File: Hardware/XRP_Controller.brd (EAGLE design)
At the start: 63.5 x 54 mm, 194 parts, among them J1 POWER_JACKPOWER_JACK_SLOT, J12 Vertical Qwiic Connector, J13 Vertical Qwiic Connector, J14 Vertical Qwiic Connector, J3 JST_6_PIN_VERTICAL, J4 JST_6_PIN_VERTICAL, J5 JST_6_PIN_VERTICAL, J6 JST_6_PIN_VERTICAL, J9 Vertical Qwiic Connector, Q3 20V/4.2A/52mΩ/1.4W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

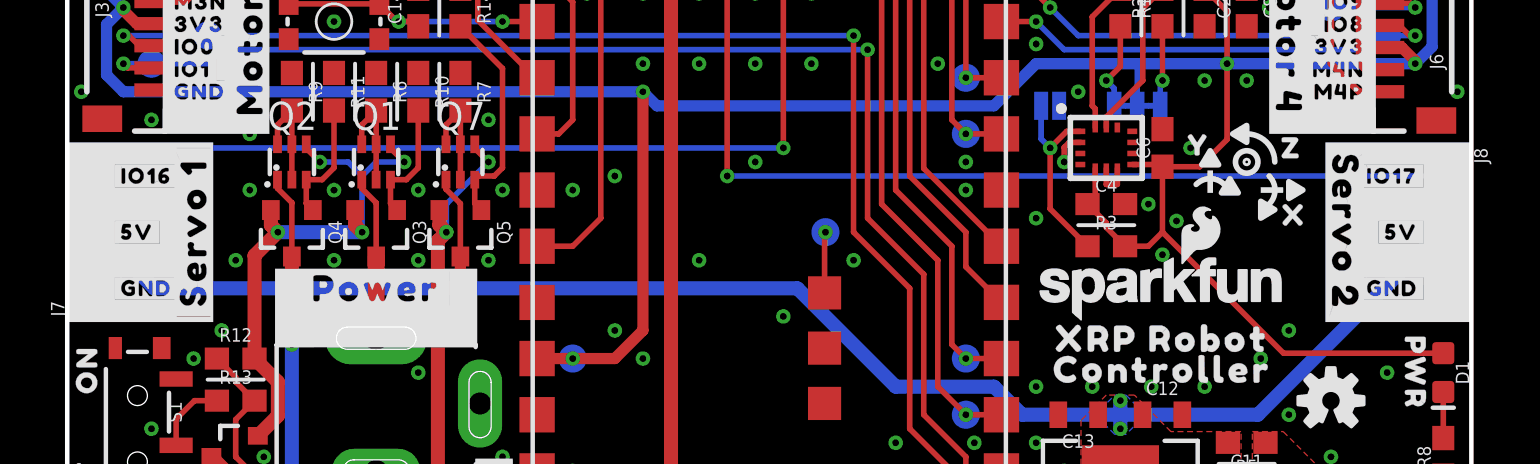
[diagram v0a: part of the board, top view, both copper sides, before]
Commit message: Nudge servo silk to improve readability
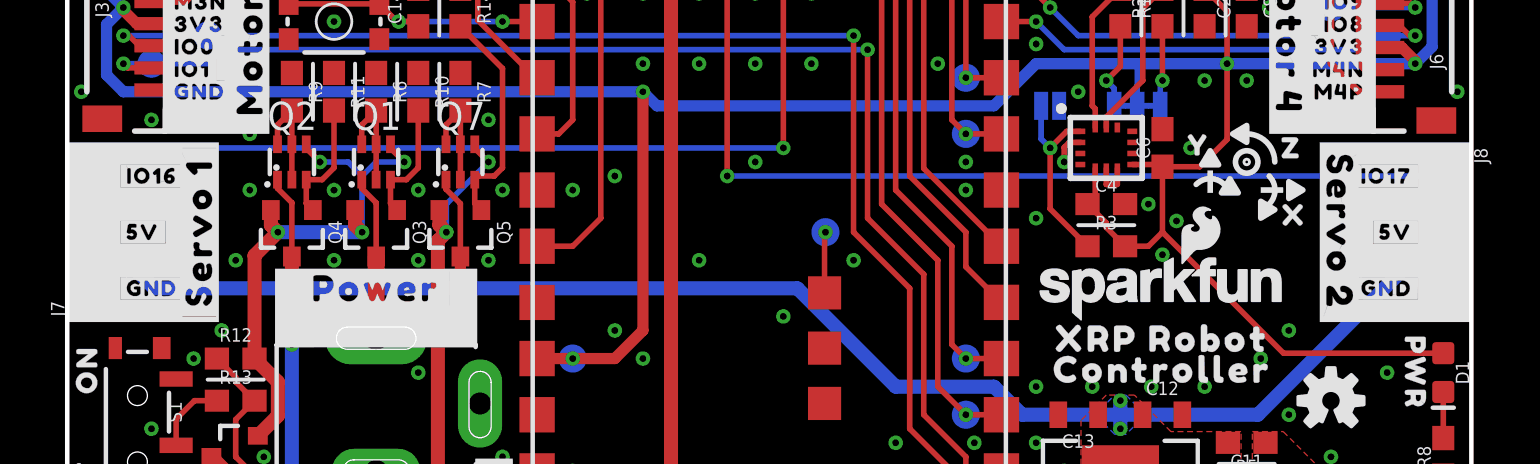
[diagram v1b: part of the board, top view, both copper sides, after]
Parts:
- moved U$11 0.25 mm to (5.97, 19.1)
- moved U$27 0.25 mm to (1.52, 19.1)
- moved U$54 0.25 mm to (2.16, 16.5)
- moved U$55 0.25 mm to (2.16, 19.1)
- moved U$56 0.25 mm to (2.16, 21.6)
- moved U$2 0.25 mm to (57.5, 19.1)
- moved U$57 0.25 mm to (61.3, 16.5)
- moved U$58 0.25 mm to (61.3, 21.6)
- moved U$59 0.25 mm to (61.3, 19.1)
- moved U$76 0.25 mm to (62.0, 19.1)
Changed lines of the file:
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@@
 <drawing>
 <settings>
-<setting alwaysvectorfont="no"/>
+<setting alwaysvectorfont="yes"/>
 <setting verticaltext="up"/>
 </settings>
@@
 <rectangle x1="52.578" y1="48.768" x2="56.642" y2="49.657" layer="21"/>
 <rectangle x1="52.578" y1="45.847" x2="56.642" y2="46.101" layer="21"/>
-<rectangle x1="58.547" y1="22.098" x2="61.341" y2="23.114" layer="21"/>
-<rectangle x1="58.547" y1="14.986" x2="61.341" y2="16.002" layer="21"/>
-<rectangle x1="58.547" y1="19.558" x2="61.341" y2="21.082" layer="21"/>
-<rectangle x1="58.547" y1="17.018" x2="61.341" y2="18.542" layer="21"/>
-<rectangle x1="58.547" y1="18.542" x2="59.309" y2="19.558" layer="21"/>
-<rectangle x1="61.341" y1="14.986" x2="63.5" y2="23.114" layer="21"/>
+<rectangle x1="58.293" y1="22.098" x2="61.087" y2="23.114" layer="21"/>
+<rectangle x1="58.293" y1="14.986" x2="61.087" y2="16.002" layer="21"/>
+<rectangle x1="58.293" y1="19.558" x2="61.087" y2="21.082" layer="21"/>
+<rectangle x1="58.293" y1="17.018" x2="61.087" y2="18.542" layer="21"/>
+<rectangle x1="58.293" y1="18.542" x2="59.055" y2="19.558" layer="21"/>
+<rectangle x1="61.087" y1="14.986" x2="63.5" y2="23.114" layer="21"/>
 <rectangle x1="51.308" y1="44.323" x2="51.435" y2="45.847" layer="21"/>
 <rectangle x1="57.785" y1="44.323" x2="57.9628" y2="45.847" layer="21"/>
@@
 <rectangle x1="7.62" y1="31.877" x2="9.144" y2="32.385" layer="21"/>
 <rectangle x1="9.017" y1="24.003" x2="9.144" y2="31.877" layer="21"/>
-<rectangle x1="56.896" y1="22.86" x2="58.547" y2="23.114" layer="21"/>
-<rectangle x1="56.896" y1="14.986" x2="58.547" y2="15.24" layer="21"/>
-<rectangle x1="56.896" y1="15.24" x2="57.023" y2="22.86" layer="21"/>
+<rectangle x1="56.642" y1="22.86" x2="58.293" y2="23.114" layer="21"/>
+<rectangle x1="56.642" y1="14.986" x2="58.293" y2="15.24" layer="21"/>
+<rectangle x1="56.642" y1="15.24" x2="56.769" y2="22.86" layer="21"/>
 <circle x="53.34" y="22.225" radius="0.0635" width="0.254" layer="21"/>
 <circle x="53.34" y="22.225" radius="0.508" width="0.254" layer="21"/>
@@
 <rectangle x1="17.272" y1="15.748" x2="18.542" y2="17.399" layer="21"/>
 <rectangle x1="10.668" y1="17.272" x2="17.272" y2="17.399" layer="21"/>
-<rectangle x1="2.159" y1="14.986" x2="4.953" y2="16.002" layer="21" rot="R180"/>
-<rectangle x1="2.159" y1="22.098" x2="4.953" y2="23.114" layer="21" rot="R180"/>
-<rectangle x1="2.159" y1="17.018" x2="4.953" y2="18.542" layer="21" rot="R180"/>
-<rectangle x1="2.159" y1="19.558" x2="4.953" y2="21.082" layer="21" rot="R180"/>
-<rectangle x1="4.191" y1="18.542" x2="4.953" y2="19.558" layer="21" rot="R180"/>
-<rectangle x1="0" y1="14.986" x2="2.159" y2="23.114" layer="21" rot="R180"/>
-<rectangle x1="4.953" y1="14.986" x2="6.604" y2="15.24" layer="21" rot="R180"/>
-<rectangle x1="4.953" y1="22.86" x2="6.604" y2="23.114" layer="21" rot="R180"/>
-<rectangle x1="6.477" y1="15.24" x2="6.604" y2="22.86" layer="21" rot="R180"/>
+<rectangle x1="2.413" y1="14.986" x2="5.207" y2="16.002" layer="21" rot="R180"/>
+<rectangle x1="2.413" y1="22.098" x2="5.207" y2="23.114" layer="21" rot="R180"/>
+<rectangle x1="2.413" y1="17.018" x2="5.207" y2="18.542" layer="21" rot="R180"/>
+<rectangle x1="2.413" y1="19.558" x2="5.207" y2="21.082" layer="21" rot="R180"/>
+<rectangle x1="4.445" y1="18.542" x2="5.207" y2="19.558" layer="21" rot="R180"/>
+<rectangle x1="0" y1="14.986" x2="2.413" y2="23.114" layer="21"/>
+<rectangle x1="5.207" y1="14.986" x2="6.858" y2="15.24" layer="21" rot="R180"/>
+<rectangle x1="5.207" y1="22.86" x2="6.858" y2="23.114" layer="21" rot="R180"/>
+<rectangle x1="6.731" y1="15.24" x2="6.858" y2="22.86" layer="21" rot="R180"/>
 <rectangle x1="4.318" y1="41.148" x2="7.62" y2="42.545" layer="21"/>
 <rectangle x1="4.318" y1="33.655" x2="7.62" y2="35.052" layer="21"/>
@@
 <element name="U$52" library="output" package="#GND#0" value="" x="46.101" y="49.149" smashed="yes" rot="R270"/>
 <element name="U$53" library="output" package="#3V3#0" value="" x="47.117" y="49.149" smashed="yes" rot="R270"/>
-<element name="U$54" library="output" package="#GND#0" value="" x="1.905" y="16.51" smashed="yes"/>
-<element name="U$55" library="output" package="#5V#0" value="" x="1.905" y="19.05" smashed="yes"/>
-<element name="U$56" library="output" package="#IO16#0" value="" x="1.905" y="21.59" smashed="yes"/>
-<element name="U$57" library="output" package="#GND#10" value="" x="61.595" y="16.51" smashed="yes"/>
-<element name="U$58" library="output" package="#IO17#0" value="" x="61.595" y="21.59" smashed="yes"/>
-<element name="U$59" library="output" package="#5V#18" value="" x="61.595" y="19.05" smashed="yes"/>
+<element name="U$54" library="output" package="#GND#0" value="" x="2.159" y="16.51" smashed="yes"/>
+<element name="U$55" library="output" package="#5V#0" value="" x="2.159" y="19.05" smashed="yes"/>
+<element name="U$56" library="output" package="#IO16#0" value="" x="2.159" y="21.59" smashed="yes"/>
+<element name="U$57" library="output" package="#GND#10" value="" x="61.341" y="16.51" smashed="yes"/>
+<element name="U$58" library="output" package="#IO17#0" value="" x="61.341" y="21.59" smashed="yes"/>
+<element name="U$59" library="output" package="#5V#18" value="" x="61.341" y="19.05" smashed="yes"/>
 <element name="Q3" library="SparkFun-DiscreteSemi" package="SOT23-3" value="20V/4.2A/52mΩ/1.4W" x="13.97" y="19.05" smashed="yes" rot="R180">
 <attribute name="NAME" x="15.621" y="19.05" size="0.6096" layer="25" font="vector" ratio="20" rot="R270" align="bottom-center"/>
@@
 <element name="U$10" library="output" package="#MOTOR_L#0" value="" x="8.255" y="38.1" smashed="yes" rot="R90"/>
 <element name="U$1" library="output" package="#MOTOR_3#0" value="" x="8.255" y="27.94" smashed="yes" rot="R90"/>
-<element name="U$11" library="output" package="#SERVO_1#0" value="" x="5.715" y="19.05" smashed="yes" rot="R90"/>
+<element name="U$11" library="output" package="#SERVO_1#0" value="" x="5.969" y="19.05" smashed="yes" rot="R90"/>
 <element name="U$8" library="output" package="#MOTOR_R#0" value="" x="55.245" y="38.1" smashed="yes" rot="R270"/>
 <element name="U$12" library="output" package="#MOTOR_4#0" value="" x="55.245" y="27.94" smashed="yes" rot="R270"/>
-<element name="U$2" library="output" package="#SERVO_2#0" value="" x="57.785" y="19.05" smashed="yes" rot="R270"/>
+<element name="U$2" library="output" package="#SERVO_2#0" value="" x="57.531" y="19.05" smashed="yes" rot="R270"/>
 <element name="U$3" library="output" package="#11V_MAX###0" value="" x="19.304" y="4.445" smashed="yes" rot="R90"/>
 <element name="C14" library="SparkFun-Capacitors" package="0603" value="0.1uF" x="15.875" y="29.21" smashed="yes" rot="R90">
@@
 <element name="TP34" library="SparkFun-Connectors" package="PAD.03X.05" value="TEST-POINT3X5" x="58.42" y="6.35" smashed="yes" rot="MR0"/>
 <element name="TP35" library="SparkFun-Connectors" package="PAD.03X.05" value="TEST-POINT3X5" x="55.88" y="6.35" smashed="yes" rot="MR0"/>
-<element name="U$27" library="output" package="#5V_#0" value="" x="1.27" y="19.05" smashed="yes" rot="MR0"/>
+<element name="U$27" library="output" package="#5V_#0" value="" x="1.524" y="19.05" smashed="yes" rot="MR0"/>
 <element name="U$26" library="output" package="#GND_#0" value="" x="1.27" y="16.51" smashed="yes" rot="MR0"/>
 <element name="U$61" library="output" package="#IO16_#0" value="" x="1.27" y="21.59" smashed="yes" rot="MR0"/>
 <element name="U$75" library="output" package="#_GND#0" value="" x="62.23" y="16.51" smashed="yes" rot="MR0"/>
-<element name="U$76" library="output" package="#_5V#0" value="" x="62.23" y="19.05" smashed="yes" rot="MR0"/>
+<element name="U$76" library="output" package="#_5V#0" value="" x="61.976" y="19.05" smashed="yes" rot="MR0"/>
 <element name="U$77" library="output" package="#_IO17#0" value="" x="62.23" y="21.59" smashed="yes" rot="MR0"/>
 <element name="U$78" library="SparkFun-Aesthetics" package="POLARITY_MARKING_CENTER_POSITIVE#JPG" value="" x="5.207" y="3.175" smashed="yes" rot="R270"/>
